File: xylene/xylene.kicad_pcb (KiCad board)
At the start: 2 copper layers, 37 x 35 mm, 26 parts, among them J1 Conn2, J2 Conn1, U1 DIP-8, U2 LMC555, U3 DIP-16

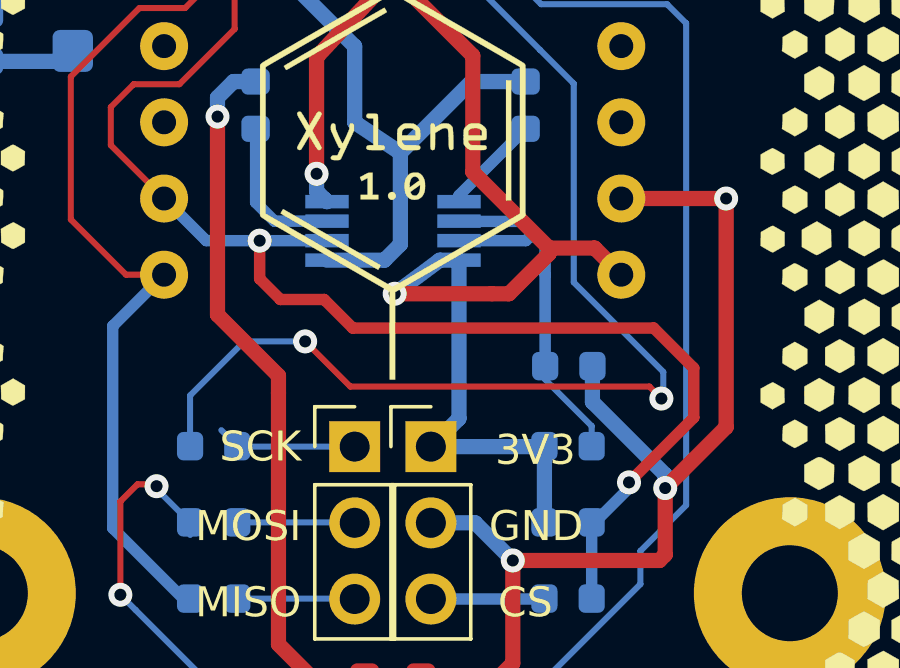
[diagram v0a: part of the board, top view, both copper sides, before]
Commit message: Change 555 to SO-8
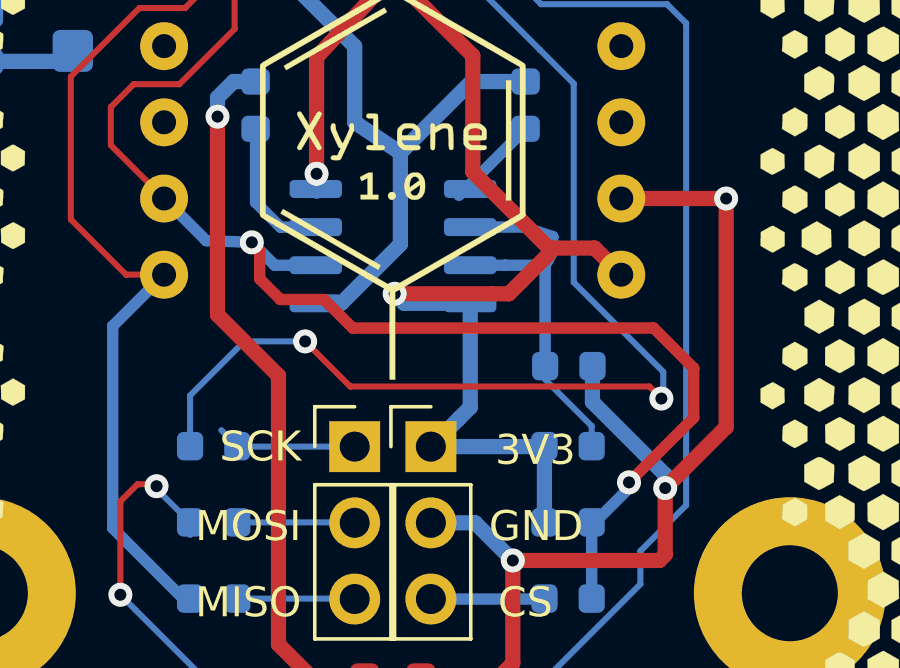
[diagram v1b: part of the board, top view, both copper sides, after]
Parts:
- U2: footprint Package_SO:VSSOP-8_3.0x3.0mm_P0.65mm -> Package_SO:SO-8_3.9x4.9mm_P1.27mm
- moved U2 0.51 mm to (107.8, 69.3)
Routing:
- net V3V3: track 84.9 -> 83.1 mm
- net GND: track 65.9 -> 66.9 mm

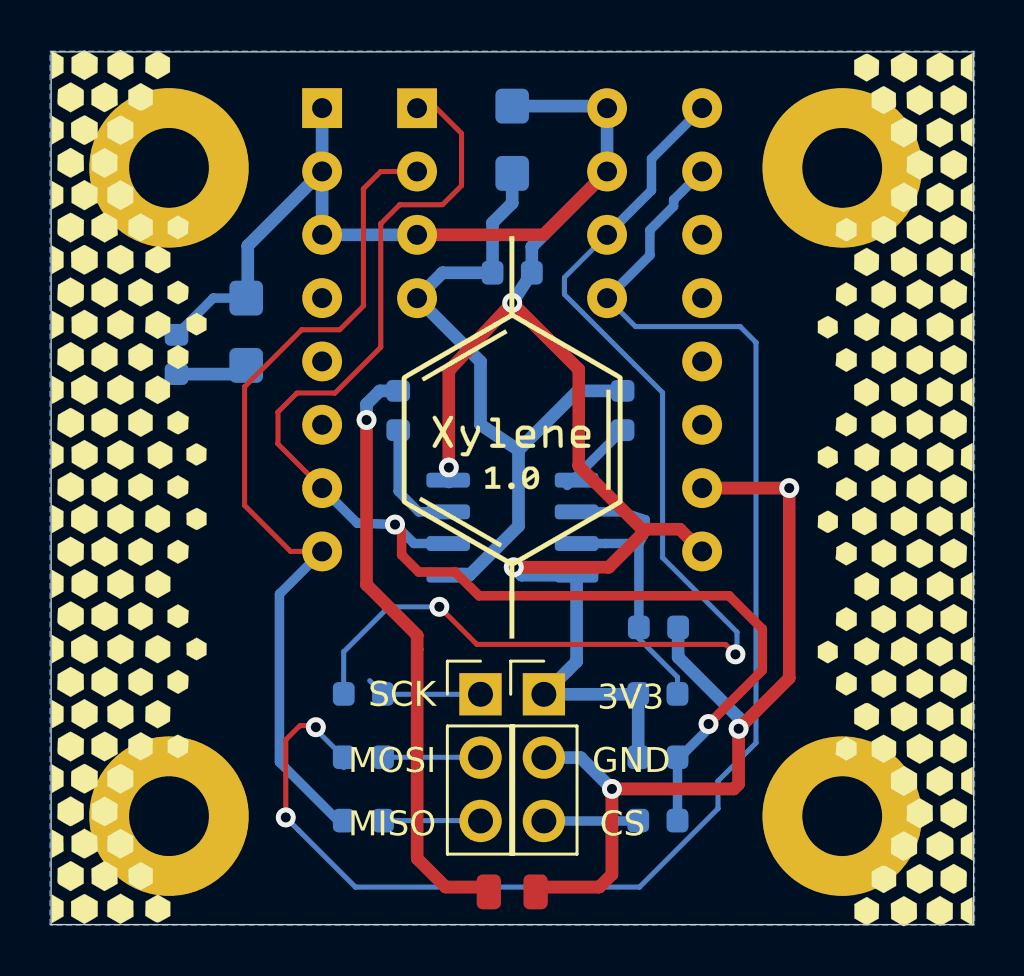
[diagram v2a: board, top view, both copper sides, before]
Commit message: Add second pins for logic analyzer
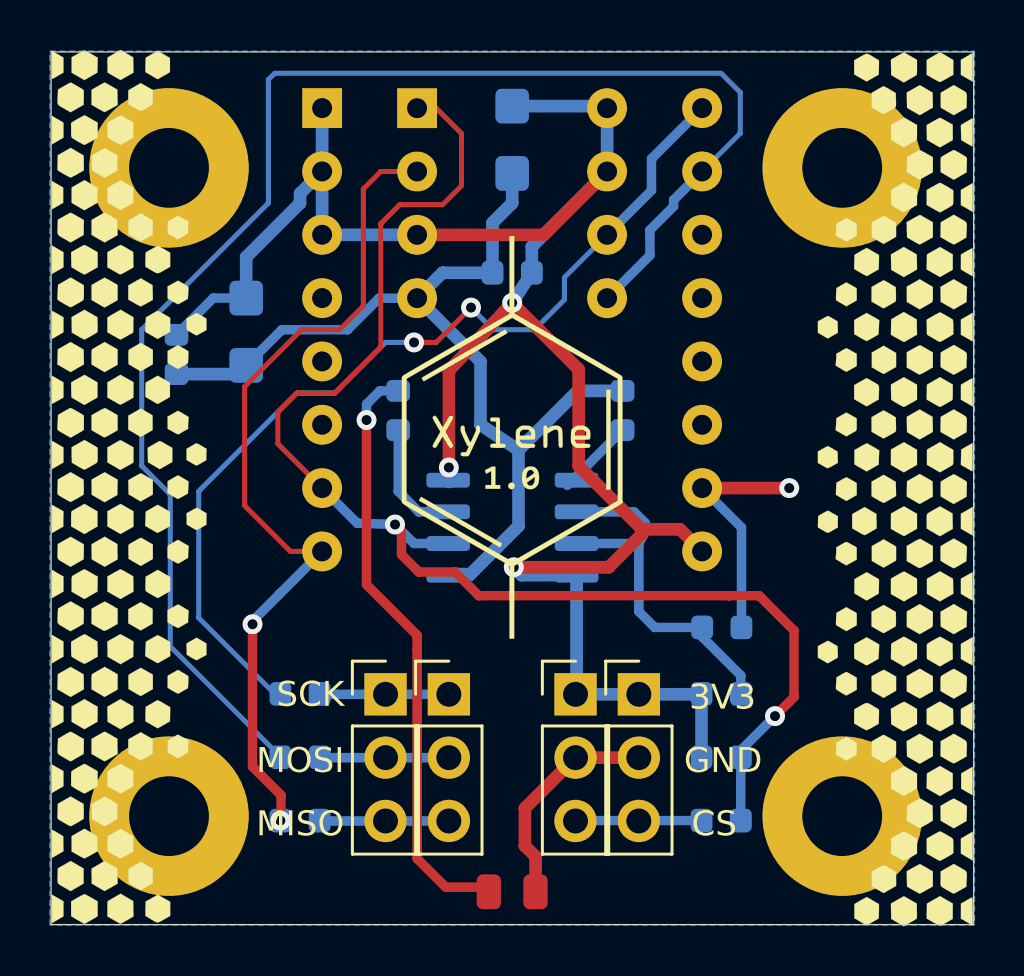
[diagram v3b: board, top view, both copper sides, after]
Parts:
- added J3: Conn2, Connector_PinHeader_2.54mm:PinHeader_1x03_P2.54mm_Vertical, F.Cu at (102.7, 76.0)
- added J4: Conn1, Connector_PinHeader_2.54mm:PinHeader_1x03_P2.54mm_Vertical, F.Cu at (112.8, 76.0)
- moved R1 2.54 mm to (116.1, 78.5)
- moved R2 2.54 mm to (116.1, 81.1)
- moved R3 2.54 mm to (99.3, 81.1)
- moved R4 2.54 mm to (99.3, 78.5)
- moved R5 2.54 mm to (99.3, 76.0)
- moved R6 2.54 mm to (116.1, 76.0)
- moved C4 2.54 mm to (116.2, 73.3)
- moved J1 1.27 mm to (105.2, 76.0)
- moved J2 1.27 mm to (110.3, 76.0)
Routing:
- net GND: track 66.9 -> 57.2 mm, vias 3 -> 1
- net SCK: track 46.3 -> 38.2 mm
- net MOSI: track 59.2 -> 61.4 mm, vias 2 -> 0
- net Net-(C4-Pad1): track 13.1 -> 15.3 mm
- net Net-(J2-Pad3): track 3.79 -> 5.08 mm
- net Net-(J1-Pad1): track 4.67 -> 5.96 mm
- net Net-(J1-Pad3): track 3.92 -> 5.19 mm
- net Net-(J1-Pad2): track 3.92 -> 5.19 mm
- net V3V3: track 83.1 -> 83.9 mm
- net CS: track 54.2 -> 54.9 mm
- net MISO: track 34.6 -> 34.3 mm, vias 0 -> 2
